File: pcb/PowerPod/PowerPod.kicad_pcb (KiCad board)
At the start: 4 copper layers, 47 x 40 mm, 67 parts, among them IC2 FUSB302MPX, IC3 CC6904SO-10A, IC4 TPS62175DQCT, IC5 ESP32-C3FH4, J1 GT-USB-7010, J2 TC2050-IDC, J3 KF350-3.5-2P, J5 Conn_01x06, U1 SRV05-4, Y2 SX25Y040000BF1T-C

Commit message: finished layout
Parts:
- added Q1: DTC143ECA-TP, SamacSys_Parts:SOT95P237X125-3N, F.Cu at (197.8, 121.9)
- added Q2: DMP3017SFG-7, SamacSys_Parts:DMP3007SFG7, F.Cu at (192.7, 121.3)
- added R19: 10k, Resistor_SMD:R_0402_1005Metric, F.Cu at (196.8, 125.4)
- added R20: 1k, Resistor_SMD:R_0402_1005Metric, F.Cu at (196.8, 124.3)
- added R21: DNF_0805, Resistor_SMD:R_0805_2012Metric_Pad1.20x1.40mm_HandSolder, F.Cu at (192.2, 125.9)
- added TP1: TestPoint, TestPoint:TestPoint_Pad_D1.0mm, F.Cu at (200.7, 118.9)
- added TP10: TestPoint, TestPoint:TestPoint_Pad_D1.0mm, F.Cu at (205.5, 136.4)
- added TP11: TestPoint, TestPoint:TestPoint_Pad_D1.0mm, F.Cu at (208.2, 101.3)
- added TP2: TestPoint, TestPoint:TestPoint_Pad_D1.0mm, F.Cu at (202.7, 119.7)
- added TP3: TestPoint, TestPoint:TestPoint_Pad_D1.0mm, F.Cu at (208.4, 107.8)
- added TP4: TestPoint, TestPoint:TestPoint_Pad_D1.0mm, F.Cu at (185.8, 105.0)
- added TP5: TestPoint, TestPoint:TestPoint_Pad_D1.0mm, F.Cu at (186.7, 102.1)
- added TP6: TestPoint, TestPoint:TestPoint_Pad_D1.0mm, F.Cu at (183.3, 132.6)
- added TP7: TestPoint, TestPoint:TestPoint_Pad_D1.0mm, F.Cu at (188.9, 122.8)
- added TP8: TestPoint, TestPoint:TestPoint_Pad_D1.0mm, F.Cu at (206.0, 132.7)
- added TP9: TestPoint, TestPoint:TestPoint_Pad_D1.0mm, F.Cu at (188.9, 127.7)
- moved S1 14.9 mm to (187.4, 134.7)
- moved R4 12.1 mm to (193.2, 116.0), turned to -90 degrees
- moved S2 9.97 mm to (184.9, 123.4)
- moved C24 9.34 mm to (201.0, 125.6), turned to 180 degrees
- moved C25 7.98 mm to (201.0, 124.6), turned to 180 degrees
- moved IC3 6.82 mm to (197.9, 128.9)
- moved C7 6.82 mm to (202.6, 127.0)
- moved C8 6.82 mm to (203.2, 128.8)
- moved R8 6.82 mm to (202.2, 128.8)
- moved D1 5.77 mm to (183.7, 116.6), turned to 180 degrees
- moved C22 5.60 mm to (191.5, 135.2), turned to -90 degrees
- moved R16 5.49 mm to (183.9, 115.3), turned to 180 degrees
- moved C1 3.31 mm to (191.6, 129.3), turned to 90 degrees
- moved J3 2.23 mm to (195.4, 136.2)
- moved C4 0.67 mm to (195.3, 108.9), turned to -90 degrees
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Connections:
- net /Current Sensor/VOUT renamed /Current Sensor + Output Control/VOUT
- net /Current Sensor/V_CURRENT renamed /Current Sensor + Output Control/V_CURRENT
- IC3 pad 1: VBUS -> Net-(Q2-D_1)
- IC3 pad 2: VBUS -> Net-(Q2-D_1)
- J5 pad 2: /Microcontroller/U0RXD -> /Microcontroller/GPIO1
- J5 pad 3: /Microcontroller/U0TXD -> /Microcontroller/GPIO0
- J5 pad 4: /Microcontroller/GPIO0 -> /Microcontroller/U0RXD
- J5 pad 5: /Microcontroller/GPIO1 -> /Microcontroller/U0TXD
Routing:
- net +3V3: track 3.85 -> 98.9 mm, vias 2 -> 13
- net VBUS: track 0.00 -> 61.1 mm, vias 0 -> 4
- net /Microcontroller/EN: track 0.00 -> 57.3 mm, vias 0 -> 5
- net /Microcontroller/GPIO9: track 0.00 -> 35.3 mm, vias 0 -> 2
- net /Microcontroller/GPIO1: track 0.00 -> 34.3 mm, vias 0 -> 1
- net /Microcontroller/GPIO3: track 0.00 -> 34.1 mm, vias 0 -> 4
- net /Microcontroller/GPIO0: track 0.00 -> 31.8 mm, vias 0 -> 1
- net /Microcontroller/U0TXD: track 0.00 -> 30.4 mm, vias 0 -> 1
- net /Microcontroller/U0RXD: track 0.00 -> 28.7 mm, vias 0 -> 1
- net /Microcontroller/USB_DP: track 1.63 -> 23.7 mm, vias 0 -> 2
- net /Microcontroller/USB_DN: track 1.65 -> 22.3 mm, vias 0 -> 2
- net /Current Sensor + Output Control/V_CURRENT: track 0.82 -> 19.3 mm, vias 1 -> 2
- net Net-(IC4-VOS): track 5.39 -> 20.8 mm, vias 1 -> 2
- net GND: track 0.00 -> 15.2 mm, vias 0 -> 22
- net Net-(Q2-D_1): track 0.00 -> 11.3 mm, vias 0 -> 2
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- added copper zone on F.Cu, net /Current Sensor + Output Control/VOUT
- added copper zone on B.Cu, net GND
- added copper zone on F.Cu, net GND
- added copper zone on In1.Cu, net GND
- added copper zone on In2.Cu, net GND
- added copper zone on F.Cu, net Net-(IC4-VOS)
- added copper zone on F.Cu, net Net-(Q2-D_1)
- added copper zone on F.Cu, net VBUS
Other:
- board size 47 x 40 mm -> 46.5 x 40 mm
- board text added: "+"
- board text added: "-"

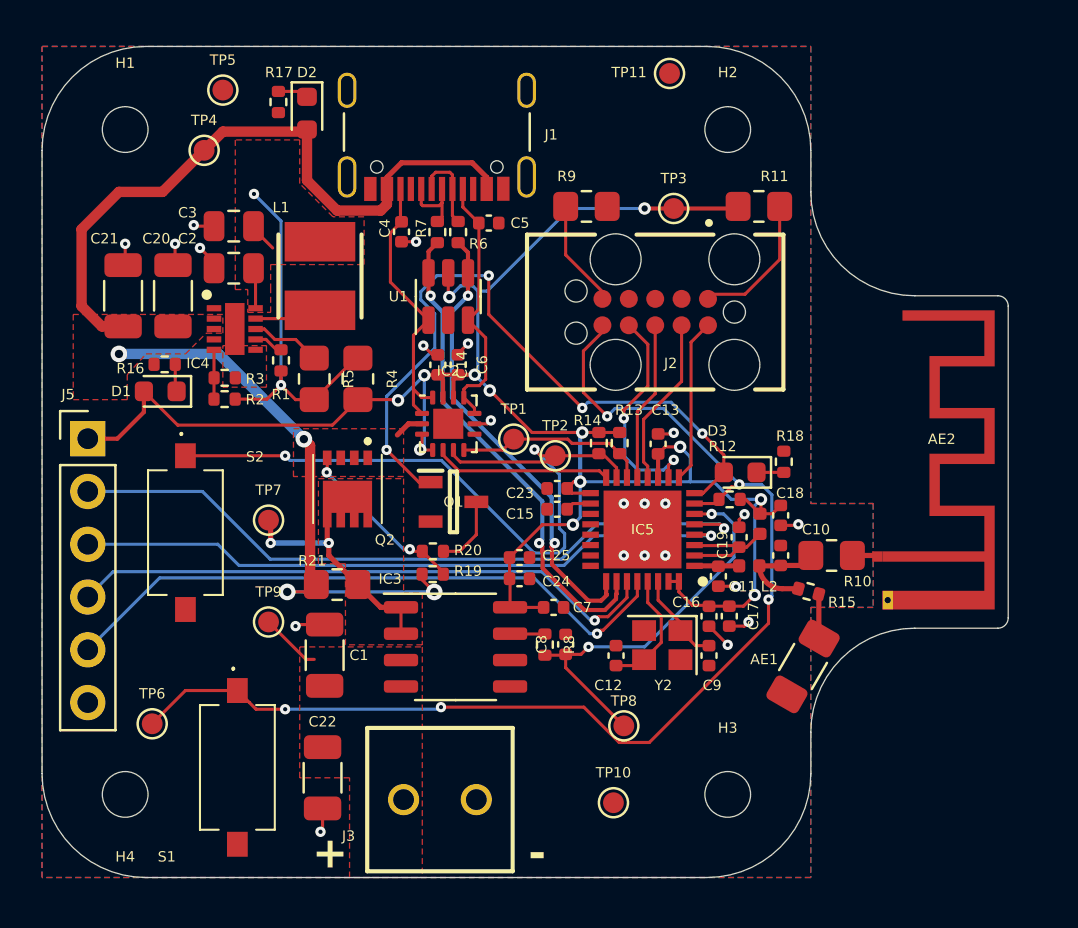
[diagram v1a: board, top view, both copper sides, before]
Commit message: changed gpio pins
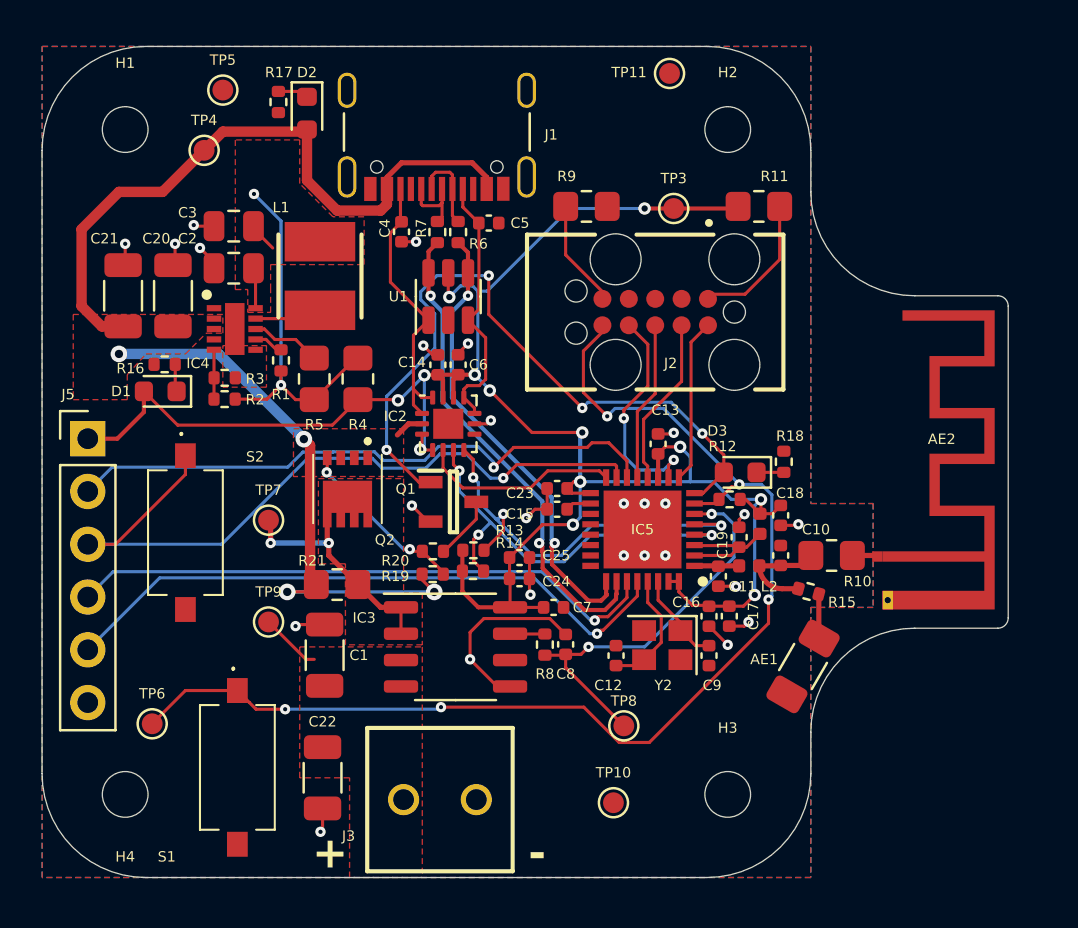
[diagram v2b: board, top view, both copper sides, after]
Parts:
- removed TP1, TP2: TestPoint, TestPoint:TestPoint_Pad_D1.0mm
- moved R13 8.73 mm to (198.8, 124.2), turned to 0 degrees
- moved R14 8.64 mm to (198.7, 125.2), turned to 0 degrees
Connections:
- IC2 pad 6: /Microcontroller/GPIO9 -> /Microcontroller/GPIO0
- IC2 pad 7: /Microcontroller/SDA -> /Microcontroller/GPIO1
- IC5 pad 14: /Microcontroller/SDA -> /Microcontroller/GPIO8
- J5 pad 2: /Microcontroller/GPIO1 -> /Microcontroller/GPIO8
- J5 pad 3: /Microcontroller/GPIO0 -> /Microcontroller/GPIO9
- R13 pad 2: /Microcontroller/SDA -> /Microcontroller/GPIO1
- R14 pad 2: /Microcontroller/GPIO9 -> /Microcontroller/GPIO0
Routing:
- net /Microcontroller/GPIO8: track 0.00 -> 29.4 mm, vias 0 -> 1
- net /Microcontroller/GPIO1: track 34.3 -> 20.0 mm, vias 1 -> 3
- net GND: track 15.2 -> 29.4 mm, vias 22 -> 26
- net /Microcontroller/GPIO0: track 31.8 -> 19.9 mm, vias 1 -> 3
- net /Microcontroller/SDA: track 9.30 -> 0.00 mm
- net +3V3: track 98.9 -> 101.7 mm
- net /Microcontroller/INT_N: track 8.30 -> 9.59 mm
- net /Microcontroller/GPIO9: track 35.3 -> 36.0 mm, vias 2 -> 1

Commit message: created production files
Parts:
- added ?: Product Stamp, personal:Product Stamp, B.Cu at (194.7, 111.9)
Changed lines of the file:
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@@
   (paper "A3")
   (title_block
-    (date "2022-11-21")
+    (date "2023-04-18")
     (rev "A")
   )
@@
     (fp_line (start 1 0.625) (end -1 0.625)
       (stroke (width 0.1) (type solid)) (layer "F.Fab"))
-    (pad "1" smd roundrect (at -1 0) (size 1.2 1.4) (layers "F.Cu" "F.Paste" "F.Mask") (roundrect_rratio 0.208333)
+    (pad "1" smd roundrect (at -1 0) (size 1.2 1.4) (layers "F.Cu" "F.Paste" "F.Mask") (roundrect_rratio 0.2083333333)
       (net 3 "VBUS") (pintype "passive"))
-    (pad "2" smd roundrect (at 1 0) (size 1.2 1.4) (layers "F.Cu" "F.Paste" "F.Mask") (roundrect_rratio 0.208333)
+    (pad "2" smd roundrect (at 1 0) (size 1.2 1.4) (layers "F.Cu" "F.Paste" "F.Mask") (roundrect_rratio 0.2083333333)
       (net 59 "Net-(Q2-D_1)") (pintype "passive"))
     (model "${KICAD6_3DMODEL_DIR}/Resistor_SMD.3dshapes/R_0805_2012Metric.wrl"
@@
     (fp_line (start 1.6 0.8) (end -1.6 0.8)
       (stroke (width 0.1) (type solid)) (layer "F.Fab"))
-    (pad "1" smd roundrect (at -1.475 0 90) (size 1.15 1.8) (layers "F.Cu" "F.Paste" "F.Mask") (roundrect_rratio 0.217391)
+    (pad "1" smd roundrect (at -1.475 0 90) (size 1.15 1.8) (layers "F.Cu" "F.Paste" "F.Mask") (roundrect_rratio 0.2173913043)
       (net 3 "VBUS") (pintype "passive"))
-    (pad "2" smd roundrect (at 1.475 0 90) (size 1.15 1.8) (layers "F.Cu" "F.Paste" "F.Mask") (roundrect_rratio 0.217391)
+    (pad "2" smd roundrect (at 1.475 0 90) (size 1.15 1.8) (layers "F.Cu" "F.Paste" "F.Mask") (roundrect_rratio 0.2173913043)
       (net 4 "GND") (pintype "passive"))
     (model "${KICAD6_3DMODEL_DIR}/Capacitor_SMD.3dshapes/C_1206_3216Metric.wrl"
@@
     (fp_line (start 1.6 0.8) (end -1.6 0.8)
       (stroke (width 0.1) (type solid)) (layer "F.Fab"))
-    (pad "1" smd roundrect (at -1.475 0 270) (size 1.15 1.8) (layers "F.Cu" "F.Paste" "F.Mask") (roundrect_rratio 0.217391)
+    (pad "1" smd roundrect (at -1.475 0 270) (size 1.15 1.8) (layers "F.Cu" "F.Paste" "F.Mask") (roundrect_rratio 0.2173913043)
       (net 8 "/Current Sensor + Output Control/VOUT") (pintype "passive"))
-    (pad "2" smd roundrect (at 1.475 0 270) (size 1.15 1.8) (layers "F.Cu" "F.Paste" "F.Mask") (roundrect_rratio 0.217391)
+    (pad "2" smd roundrect (at 1.475 0 270) (size 1.15 1.8) (layers "F.Cu" "F.Paste" "F.Mask") (roundrect_rratio 0.2173913043)
       (net 4 "GND") (pintype "passive"))
     (model "${KICAD6_3DMODEL_DIR}/Capacitor_SMD.3dshapes/C_1206_3216Metric.wrl"
@@
     (fp_line (start 1 0.625) (end -1 0.625)
       (stroke (width 0.1) (type solid)) (layer "F.Fab"))
-    (pad "1" smd roundrect (at -1 0) (size 1.2 1.4) (layers "F.Cu" "F.Paste" "F.Mask") (roundrect_rratio 0.208333)
+    (pad "1" smd roundrect (at -1 0) (size 1.2 1.4) (layers "F.Cu" "F.Paste" "F.Mask") (roundrect_rratio 0.2083333333)
       (net 10 "Net-(C10-Pad1)") (pintype "passive"))
-    (pad "2" smd roundrect (at 1 0) (size 1.2 1.4) (layers "F.Cu" "F.Paste" "F.Mask") (roundrect_rratio 0.208333)
+    (pad "2" smd roundrect (at 1 0) (size 1.2 1.4) (layers "F.Cu" "F.Paste" "F.Mask") (roundrect_rratio 0.2083333333)
       (net 15 "Net-(AE2-A)") (pintype "passive"))
     (model "${KICAD6_3DMODEL_DIR}/Resistor_SMD.3dshapes/R_0805_2012Metric.wrl"
@@
     (fp_line (start 1 0.625) (end -1 0.625)
       (stroke (width 0.1) (type solid)) (layer "F.Fab"))
-    (pad "1" smd roundrect (at -1 0) (size 1.2 1.4) (layers "F.Cu" "F.Paste" "F.Mask") (roundrect_rratio 0.208333)
+    (pad "1" smd roundrect (at -1 0) (size 1.2 1.4) (layers "F.Cu" "F.Paste" "F.Mask") (roundrect_rratio 0.2083333333)
       (net 50 "Net-(J2-GNDDetect)") (pintype "passive"))
-    (pad "2" smd roundrect (at 1 0) (size 1.2 1.4) (layers "F.Cu" "F.Paste" "F.Mask") (roundrect_rratio 0.208333)
+    (pad "2" smd roundrect (at 1 0) (size 1.2 1.4) (layers "F.Cu" "F.Paste" "F.Mask") (roundrect_rratio 0.2083333333)
       (net 4 "GND") (pintype "passive"))
     (model "${KICAD6_3DMODEL_DIR}/Resistor_SMD.3dshapes/R_0805_2012Metric.wrl"
@@
     (fp_line (start 1 0.625) (end -1 0.625)
       (stroke (width 0.1) (type solid)) (layer "F.Fab"))
-    (pad "1" smd roundrect (at -1 0 270) (size 1.2 1.4) (layers "F.Cu" "F.Paste" "F.Mask") (roundrect_rratio 0.208333)
+    (pad "1" smd roundrect (at -1 0 270) (size 1.2 1.4) (layers "F.Cu" "F.Paste" "F.Mask") (roundrect_rratio 0.2083333333)
       (net 22 "Net-(IC4-SLEEP)") (pintype "passive"))
-    (pad "2" smd roundrect (at 1 0 270) (size 1.2 1.4) (layers "F.Cu" "F.Paste" "F.Mask") (roundrect_rratio 0.208333)
+    (pad "2" smd roundrect (at 1 0 270) (size 1.2 1.4) (layers "F.Cu" "F.Paste" "F.Mask") (roundrect_rratio 0.2083333333)
       (net 51 "Net-(IC4-VOS)") (pintype "passive"))
     (model "${KICAD6_3DMODEL_DIR}/Resistor_SMD.3dshapes/R_0805_2012Metric.wrl"
@@
     (fp_line (start 1.6 0.8) (end -1.6 0.8)
       (stroke (width 0.1) (type solid)) (layer "F.Fab"))
-    (pad "1" smd roundrect (at -1.475 0 90) (size 1.15 1.8) (layers "F.Cu" "F.Paste" "F.Mask") (roundrect_rratio 0.217391)
+    (pad "1" smd roundrect (at -1.475 0 90) (size 1.15 1.8) (layers "F.Cu" "F.Paste" "F.Mask") (roundrect_rratio 0.2173913043)
       (net 3 "VBUS") (pintype "passive"))
-    (pad "2" smd roundrect (at 1.475 0 90) (size 1.15 1.8) (layers "F.Cu" "F.Paste" "F.Mask") (roundrect_rratio 0.217391)
+    (pad "2" smd roundrect (at 1.475 0 90) (size 1.15 1.8) (layers "F.Cu" "F.Paste" "F.Mask") (roundrect_rratio 0.2173913043)
       (net 4 "GND") (pintype "passive"))
     (model "${KICAD6_3DMODEL_DIR}/Capacitor_SMD.3dshapes/C_1206_3216Metric.wrl"
@@
     (fp_line (start 1 0.625) (end -1 0.625)
       (stroke (width 0.1) (type solid)) (layer "F.Fab"))
-    (pad "1" smd roundrect (at -1 0) (size 1.2 1.4) (layers "F.Cu" "F.Paste" "F.Mask") (roundrect_rratio 0.208333)
+    (pad "1" smd roundrect (at -1 0) (size 1.2 1.4) (layers "F.Cu" "F.Paste" "F.Mask") (roundrect_rratio 0.2083333333)
       (net 5 "+3V3") (pintype "passive"))
-    (pad "2" smd roundrect (at 1 0) (size 1.2 1.4) (layers "F.Cu" "F.Paste" "F.Mask") (roundrect_rratio 0.208333)
+    (pad "2" smd roundrect (at 1 0) (size 1.2 1.4) (layers "F.Cu" "F.Paste" "F.Mask") (roundrect_rratio 0.2083333333)
       (net 48 "Net-(J2-VTref)") (pintype "passive"))
     (model "${KICAD6_3DMODEL_DIR}/Resistor_SMD.3dshapes/R_0805_2012Metric.wrl"
@@
     (fp_line (start 1.6 0.8) (end -1.6 0.8)
       (stroke (width 0.1) (type solid)) (layer "F.Fab"))
-    (pad "1" smd roundrect (at -1.55 0 60) (size 1.3 1.75) (layers "F.Cu" "F.Paste" "F.Mask") (roundrect_rratio 0.192308)
+    (pad "1" smd roundrect (at -1.55 0 60) (size 1.3 1.75) (layers "F.Cu" "F.Paste" "F.Mask") (roundrect_rratio 0.1923076923)
       (net 1 "unconnected-(AE1-FEED-Pad1)") (pinfunction "FEED") (pintype "input+no_connect"))
-    (pad "2" smd roundrect (at 1.55 0 60) (size 1.3 1.75) (layers "F.Cu" "F.Paste" "F.Mask") (roundrect_rratio 0.192308)
+    (pad "2" smd roundrect (at 1.55 0 60) (size 1.3 1.75) (layers "F.Cu" "F.Paste" "F.Mask") (roundrect_rratio 0.1923076923)
       (net 2 "Net-(AE1-PCB_Trace)") (pinfunction "PCB_Trace") (pintype "passive"))
     (model "${KICAD6_3DMODEL_DIR}/Resistor_SMD.3dshapes/R_1206_3216Metric.wrl"
@@
     (fp_line (start 1 0.625) (end -1 0.625)
       (stroke (width 0.1) (type solid)) (layer "F.Fab"))
-    (pad "1" smd roundrect (at -1 0 270) (size 1.2 1.4) (layers "F.Cu" "F.Paste" "F.Mask") (roundrect_rratio 0.208333)
+    (pad "1" smd roundrect (at -1 0 270) (size 1.2 1.4) (layers "F.Cu" "F.Paste" "F.Mask") (roundrect_rratio 0.2083333333)
       (net 51 "Net-(IC4-VOS)") (pintype "passive"))
-    (pad "2" smd roundrect (at 1 0 270) (size 1.2 1.4) (layers "F.Cu" "F.Paste" "F.Mask") (roundrect_rratio 0.208333)
+    (pad "2" smd roundrect (at 1 0 270) (size 1.2 1.4) (layers "F.Cu" "F.Paste" "F.Mask") (roundrect_rratio 0.2083333333)
       (net 5 "+3V3") (pintype "passive"))
     (model "${KICAD6_3DMODEL_DIR}/Resistor_SMD.3dshapes/R_0805_2012Metric.wrl"
@@
     (fp_line (start 1.6 0.8) (end -1.6 0.8)
       (stroke (width 0.1) (type solid)) (layer "F.Fab"))
-    (pad "1" smd roundrect (at -1.475 0 90) (size 1.15 1.8) (layers "F.Cu" "F.Paste" "F.Mask") (roundrect_rratio 0.217391)
+    (pad "1" smd roundrect (at -1.475 0 90) (size 1.15 1.8) (layers "F.Cu" "F.Paste" "F.Mask") (roundrect_rratio 0.2173913043)
       (net 8 "/Current Sensor + Output Control/VOUT") (pintype "passive"))
-    (pad "2" smd roundrect (at 1.475 0 90) (size 1.15 1.8) (layers "F.Cu" "F.Paste" "F.Mask") (roundrect_rratio 0.217391)
+    (pad "2" smd roundrect (at 1.475 0 90) (size 1.15 1.8) (layers "F.Cu" "F.Paste" "F.Mask") (roundrect_rratio 0.2173913043)
       (net 4 "GND") (pintype "passive"))
     (model "${KICAD6_3DMODEL_DIR}/Capacitor_SMD.3dshapes/C_1206_3216Metric.wrl"
@@
     )
   )
+  (footprint "personal:Product Stamp" (layer "B.Cu")
+    (at 194.7 111.9 180)
+    (attr smd)
+    (fp_text reference "" (at 0 0.5 unlocked) (layer "B.SilkS")
+        (effects (font (size 1 1) (thickness 0.15)) (justify mirror))
+    )
+    (fp_text value "Product Stamp" (at 0 -3 unlocked) (layer "B.Fab")
+        (effects (font (size 1 1) (thickness 0.15)) (justify mirror))
+    )
+    (fp_text user "elektroThing" (at 0 -1.75 unlocked) (layer "B.SilkS")
+        (effects (font (size 1 1) (thickness 0.15)) (justify left mirror))
+    )
+    (fp_text user "April 2023" (at 0 -3.5 unlocked) (layer "B.SilkS")
+        (effects (font (size 1 1) (thickness 0.15)) (justify left mirror))
+    )
+    (fp_text user "Rev A" (at 0 -5.25 unlocked) (layer "B.SilkS")
+        (effects (font (size 1 1) (thickness 0.15)) (justify left mirror))
+    )
+    (fp_text user "PowerPod" (at 0 0 unlocked) (layer "B.SilkS")
+        (effects (font (size 1 1) (thickness 0.15)) (justify left mirror))
+    )
+  )
